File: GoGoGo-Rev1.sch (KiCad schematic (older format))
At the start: 0 parts

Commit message: Finished simple schematic, added netlists
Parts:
- added C? (x2): C, symbol C
- added P?: CONN_01X06, symbol CONN_01X06
- added P?: CONN_01X02, symbol CONN_01X02
- added U?: DRV8837DSGR, symbol DRV8837DSGR
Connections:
- new net: C?.1, C?.1, P?.6 (P6), U?.1 (VM)
- new net: P?.1 (P1), U?.2 (Out1)
- new net: P?.2 (P2), U?.3 (Out2)
- new net: P?.2 (P2), U?.5 (IN2)
- new net: P?.3 (P3), U?.6 (IN1)
- new net: P?.1 (P1), U?.7 (nSleep)
- new net: P?.5 (P5), U?.8 (VCC)
- new net GND: C?.2, C?.2, P?.4 (P4), U?.4 (GND)
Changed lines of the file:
@@
 LIBS:contrib
 LIBS:valves
+LIBS:GoGoGo
+LIBS:GoGoGo-Rev1-cache
 EELAYER 25 0
 EELAYER END
@@
 Comment4 ""
 $EndDescr
+$Comp
+L DRV8837DSGR U?
+U 1 1 557C7CEE
+P 5550 4200
+F 0 "U?" H 5900 3650 60  0000 C CNN
+F 1 "DRV8837DSGR" H 5550 4200 60  0000 C CNN
+F 2 "" H 5250 4150 60  0000 C CNN
+F 3 "" H 5250 4150 60  0000 C CNN
+	1    5550 4200
+	1    0    0    -1
+$EndComp
+$Comp
+L CONN_01X06 P?
+U 1 1 557C7D40
+P 3350 2750
+F 0 "P?" H 3350 3100 50  0000 C CNN
+F 1 "CONN_01X06" V 3450 2750 50  0000 C CNN
+F 2 "" H 3350 2750 60  0000 C CNN
+F 3 "" H 3350 2750 60  0000 C CNN
+	1    3350 2750
+	-1   0    0    1
+$EndComp
+Wire Wire Line
+	3550 2500 5750 2500
+Wire Wire Line
+	5750 2500 5750 3500
+Wire Wire Line
+	3550 2600 5450 2600
+Wire Wire Line
+	5450 2600 5450 3500
+Wire Wire Line
+	3550 2700 4500 2700
+Wire Wire Line
+	4500 2700 4500 3450
+$Comp
+L GND #PWR?
+U 1 1 557C7E63
+P 4500 3450
+F 0 "#PWR?" H 4500 3200 50  0001 C CNN
+F 1 "GND" H 4500 3300 50  0000 C CNN
+F 2 "" H 4500 3450 60  0000 C CNN
+F 3 "" H 4500 3450 60  0000 C CNN
+	1    4500 3450
+	1    0    0    -1
+$EndComp
+$Comp
+L GND #PWR?
+U 1 1 557C7E7B
+P 5550 4900
+F 0 "#PWR?" H 5550 4650 50  0001 C CNN
+F 1 "GND" H 5550 4750 50  0000 C CNN
+F 2 "" H 5550 4900 60  0000 C CNN
+F 3 "" H 5550 4900 60  0000 C CNN
+	1    5550 4900
+	1    0    0    -1
+$EndComp
+Wire Wire Line
+	3550 3000 3950 3000
+Wire Wire Line
+	3950 3000 3950 4400
+Wire Wire Line
+	3950 4400 4950 4400
+Wire Wire Line
+	4950 4050 4100 4050
+Wire Wire Line
+	4100 4050 4100 2900
+Wire Wire Line
+	4100 2900 3550 2900
+Wire Wire Line
+	4950 3900 4250 3900
+Wire Wire Line
+	4250 3900 4250 2800
+Wire Wire Line
+	4250 2800 3550 2800
+$Comp
+L CONN_01X02 P?
+U 1 1 557C7F48
+P 7600 4000
+F 0 "P?" H 7600 4150 50  0000 C CNN
+F 1 "CONN_01X02" V 7700 4000 50  0000 C CNN
+F 2 "" H 7600 4000 60  0000 C CNN
+F 3 "" H 7600 4000 60  0000 C CNN
+	1    7600 4000
+	1    0    0    -1
+$EndComp
+Wire Wire Line
+	7400 3950 6150 3950
+Wire Wire Line
+	6150 3950 6150 3900
+Wire Wire Line
+	6150 4500 6950 4500
+Wire Wire Line
+	6950 4500 6950 4050
+Wire Wire Line
+	6950 4050 7400 4050
+$Comp
+L C C?
+U 1 1 557C800B
+P 4800 2950
+F 0 "C?" H 4825 3050 50  0000 L CNN
+F 1 "C" H 4825 2850 50  0000 L CNN
+F 2 "" H 4838 2800 30  0000 C CNN
+F 3 "" H 4800 2950 60  0000 C CNN
+	1    4800 2950
+	1    0    0    -1
+$EndComp
+$Comp
+L C C?
+U 1 1 557C8092
+P 5150 2950
+F 0 "C?" H 5175 3050 50  0000 L CNN
+F 1 "C" H 5175 2850 50  0000 L CNN
+F 2 "" H 5188 2800 30  0000 C CNN
+F 3 "" H 5150 2950 60  0000 C CNN
+	1    5150 2950
+	1    0    0    -1
+$EndComp
+Wire Wire Line
+	5150 2800 5150 2500
+Connection ~ 5150 2500
+Wire Wire Line
+	4800 2800 4800 2500
+Connection ~ 4800 2500
+Wire Wire Line
+	4800 3100 4800 3250
+Wire Wire Line
+	4800 3250 4500 3250
+Connection ~ 4500 3250
+Wire Wire Line
+	5150 3100 5150 3350
+Wire Wire Line
+	5150 3350 4500 3350
+Connection ~ 4500 3350
 $EndSCHEMATC

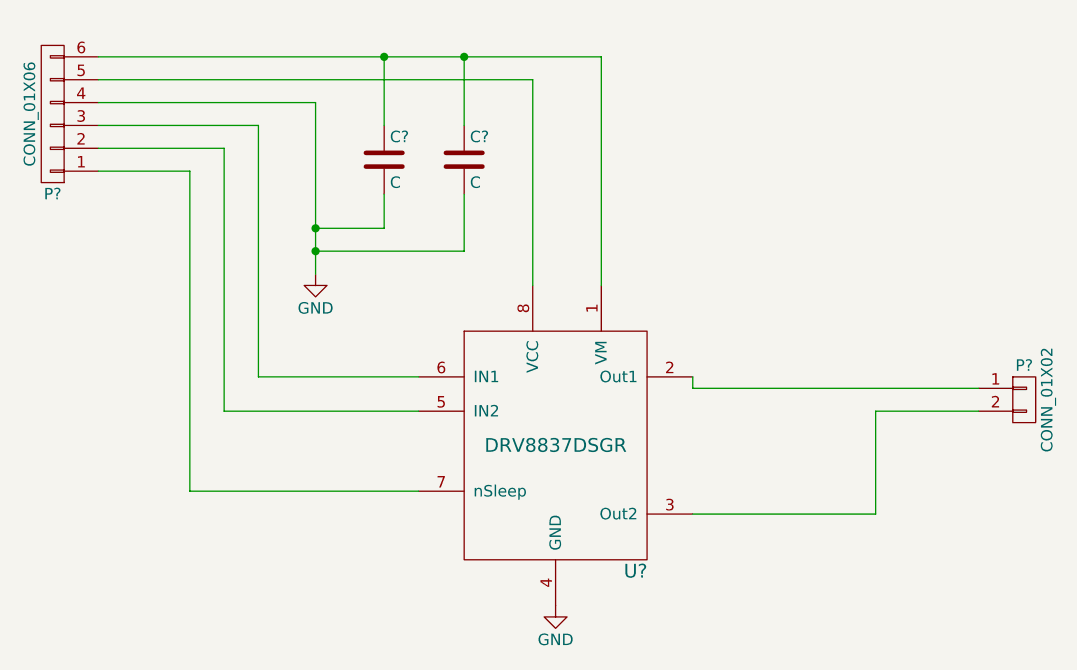
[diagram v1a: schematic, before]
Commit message: Added PWSON footprint
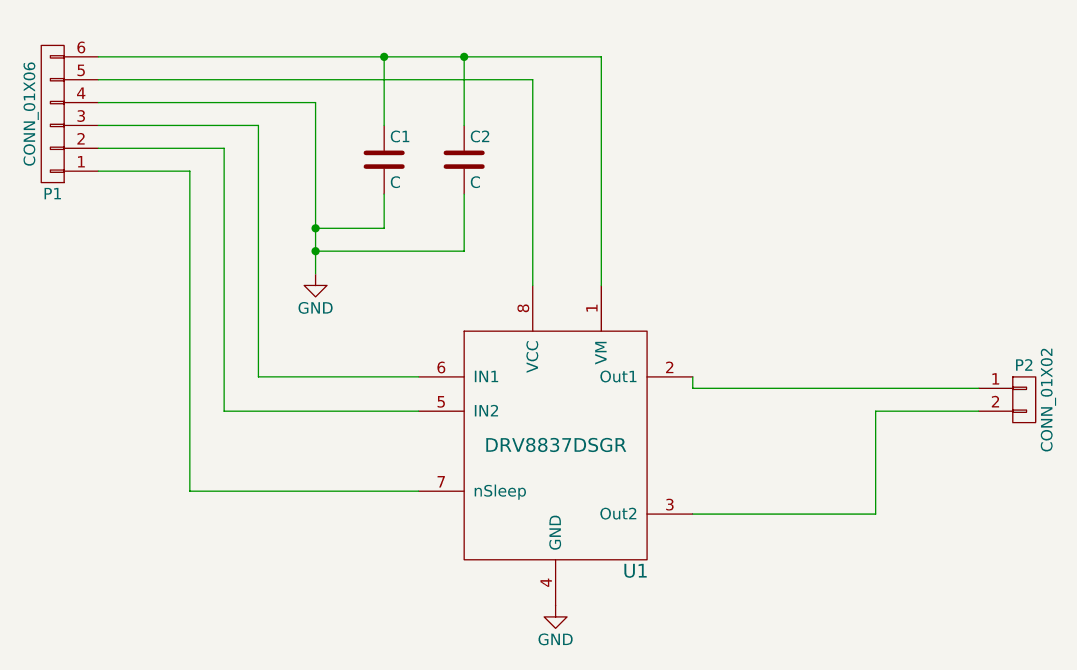
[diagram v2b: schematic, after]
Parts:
- gave numbers to parts that had none: 5
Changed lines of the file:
@@
 $EndDescr
 $Comp
-L DRV8837DSGR U?
+L DRV8837DSGR U1
 U 1 1 557C7CEE
 P 5550 4200
-F 0 "U?" H 5900 3650 60  0000 C CNN
+F 0 "U1" H 5900 3650 60  0000 C CNN
 F 1 "DRV8837DSGR" H 5550 4200 60  0000 C CNN
 F 2 "" H 5250 4150 60  0000 C CNN
@@
 $EndComp
 $Comp
-L CONN_01X06 P?
+L CONN_01X06 P1
 U 1 1 557C7D40
 P 3350 2750
-F 0 "P?" H 3350 3100 50  0000 C CNN
+F 0 "P1" H 3350 3100 50  0000 C CNN
 F 1 "CONN_01X06" V 3450 2750 50  0000 C CNN
 F 2 "" H 3350 2750 60  0000 C CNN
@@
 	4500 2700 4500 3450
 $Comp
-L GND #PWR?
+L GND #PWR01
 U 1 1 557C7E63
 P 4500 3450
-F 0 "#PWR?" H 4500 3200 50  0001 C CNN
+F 0 "#PWR01" H 4500 3200 50  0001 C CNN
 F 1 "GND" H 4500 3300 50  0000 C CNN
 F 2 "" H 4500 3450 60  0000 C CNN
@@
 $EndComp
 $Comp
-L GND #PWR?
+L GND #PWR02
 U 1 1 557C7E7B
 P 5550 4900
-F 0 "#PWR?" H 5550 4650 50  0001 C CNN
+F 0 "#PWR02" H 5550 4650 50  0001 C CNN
 F 1 "GND" H 5550 4750 50  0000 C CNN
 F 2 "" H 5550 4900 60  0000 C CNN
@@
 	4250 2800 3550 2800
 $Comp
-L CONN_01X02 P?
+L CONN_01X02 P2
 U 1 1 557C7F48
 P 7600 4000
-F 0 "P?" H 7600 4150 50  0000 C CNN
+F 0 "P2" H 7600 4150 50  0000 C CNN
 F 1 "CONN_01X02" V 7700 4000 50  0000 C CNN
 F 2 "" H 7600 4000 60  0000 C CNN
@@
 	6950 4050 7400 4050
 $Comp
-L C C?
+L C C1
 U 1 1 557C800B
 P 4800 2950
-F 0 "C?" H 4825 3050 50  0000 L CNN
+F 0 "C1" H 4825 3050 50  0000 L CNN
 F 1 "C" H 4825 2850 50  0000 L CNN
 F 2 "" H 4838 2800 30  0000 C CNN
@@
 $EndComp
 $Comp
-L C C?
+L C C2
 U 1 1 557C8092
 P 5150 2950
-F 0 "C?" H 5175 3050 50  0000 L CNN
+F 0 "C2" H 5175 3050 50  0000 L CNN
 F 1 "C" H 5175 2850 50  0000 L CNN
 F 2 "" H 5188 2800 30  0000 C CNN

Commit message: PCB finished
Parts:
- removed P1: CONN_01X06, symbol CONN_01X06
- added P1, P3: CONN_01X03, Pin_Headers:Pin_Header_Straight_1x03, symbol CONN_01X03
- C1, C2: footprint (none) -> Capacitors_SMD:C_0603
- P2: footprint (none) -> Pin_Headers:Pin_Header_Straight_1x02
- U1: footprint (none) -> GoGoGo:PWSON-N8
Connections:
- net GND: now also P1.1 (P1)
- net VM: now reaches C2.1, U1.1 (VM)
- net VM: now also P1.3 (P3); no longer C1.1
- net OUT1: now reaches P2.1 (P1), U1.2 (Out1)
- net OUT2: now reaches P2.2 (P2), U1.3 (Out2)
- net IN2: now reaches U1.5 (IN2)
- net IN2: now also P3.1 (P1)
- net IN1: now reaches U1.6 (IN1)
- net IN1: now also P3.2 (P2)
- net nSleep: now reaches U1.7 (nSleep)
- net nSleep: now also P3.3 (P3)
- net VIN: now reaches U1.8 (VCC)
- net VIN: now also C1.1, P1.2 (P2)
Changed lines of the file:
@@
 F 0 "U1" H 5900 3650 60  0000 C CNN
 F 1 "DRV8837DSGR" H 5550 4200 60  0000 C CNN
-F 2 "" H 5250 4150 60  0000 C CNN
+F 2 "GoGoGo:PWSON-N8" H 5250 4150 60  0001 C CNN
 F 3 "" H 5250 4150 60  0000 C CNN
 	1    5550 4200
 	1    0    0    -1
-$EndComp
-$Comp
-L CONN_01X06 P1
-U 1 1 557C7D40
-P 3350 2750
-F 0 "P1" H 3350 3100 50  0000 C CNN
-F 1 "CONN_01X06" V 3450 2750 50  0000 C CNN
-F 2 "" H 3350 2750 60  0000 C CNN
-F 3 "" H 3350 2750 60  0000 C CNN
-	1    3350 2750
-	-1   0    0    1
 $EndComp
 Wire Wire Line
@@
 $EndComp
 Wire Wire Line
-	3550 3000 3950 3000
-Wire Wire Line
-	3950 3000 3950 4400
-Wire Wire Line
 	3950 4400 4950 4400
 Wire Wire Line
 	4950 4050 4100 4050
 Wire Wire Line
-	4100 4050 4100 2900
-Wire Wire Line
-	4100 2900 3550 2900
-Wire Wire Line
 	4950 3900 4250 3900
-Wire Wire Line
-	4250 3900 4250 2800
-Wire Wire Line
-	4250 2800 3550 2800
 $Comp
 L CONN_01X02 P2
@@
 F 0 "P2" H 7600 4150 50  0000 C CNN
 F 1 "CONN_01X02" V 7700 4000 50  0000 C CNN
-F 2 "" H 7600 4000 60  0000 C CNN
+F 2 "Pin_Headers:Pin_Header_Straight_1x02" H 7600 4000 60  0001 C CNN
 F 3 "" H 7600 4000 60  0000 C CNN
 	1    7600 4000
@@
 F 0 "C1" H 4825 3050 50  0000 L CNN
 F 1 "C" H 4825 2850 50  0000 L CNN
-F 2 "" H 4838 2800 30  0000 C CNN
+F 2 "Capacitors_SMD:C_0603" H 4838 2800 30  0001 C CNN
 F 3 "" H 4800 2950 60  0000 C CNN
 	1    4800 2950
@@
 F 0 "C2" H 5175 3050 50  0000 L CNN
 F 1 "C" H 5175 2850 50  0000 L CNN
-F 2 "" H 5188 2800 30  0000 C CNN
+F 2 "Capacitors_SMD:C_0603" H 5188 2800 30  0001 C CNN
 F 3 "" H 5150 2950 60  0000 C CNN
 	1    5150 2950
@@
 	5150 2800 5150 2500
 Connection ~ 5150 2500
-Wire Wire Line
-	4800 2800 4800 2500
-Connection ~ 4800 2500
 Wire Wire Line
 	4800 3100 4800 3250
@@
 	5150 3350 4500 3350
 Connection ~ 4500 3350
+Text Label 6450 3950 0    60   ~ 0
+OUT1
+Text Label 6450 4500 0    60   ~ 0
+OUT2
+Text Label 5400 2500 0    60   ~ 0
+VM
+Text Label 5300 2600 0    60   ~ 0
+VIN
+Text Label 4450 3900 0    60   ~ 0
+IN1
+Text Label 4450 4050 0    60   ~ 0
+IN2
+Text Label 4450 4400 0    60   ~ 0
+nSleep
+Wire Wire Line
+	4800 2800 4800 2600
+Connection ~ 4800 2600
+Wire Wire Line
+	3550 2900 4250 2900
+Wire Wire Line
+	4250 2900 4250 3900
+Wire Wire Line
+	3550 3000 4100 3000
+Wire Wire Line
+	4100 3000 4100 4050
+Wire Wire Line
+	3950 4400 3950 2800
+Wire Wire Line
+	3950 2800 3550 2800
+$Comp
+L CONN_01X03 P1
+U 1 1 557C8C55
+P 3350 2600
+F 0 "P1" H 3350 2800 50  0000 C CNN
+F 1 "CONN_01X03" V 3450 2600 50  0000 C CNN
+F 2 "Pin_Headers:Pin_Header_Straight_1x03" H 3350 2600 60  0001 C CNN
+F 3 "" H 3350 2600 60  0000 C CNN
+	1    3350 2600
+	-1   0    0    1
+$EndComp
+$Comp
+L CONN_01X03 P3
+U 1 1 557C8CB0
+P 3350 2900
+F 0 "P3" H 3350 3100 50  0000 C CNN
+F 1 "CONN_01X03" V 3450 2900 50  0000 C CNN
+F 2 "Pin_Headers:Pin_Header_Straight_1x03" H 3350 2900 60  0001 C CNN
+F 3 "" H 3350 2900 60  0000 C CNN
+	1    3350 2900
+	-1   0    0    1
+$EndComp
 $EndSCHEMATC
